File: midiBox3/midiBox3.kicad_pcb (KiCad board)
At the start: 2 copper layers, 100 x 100 mm, 117 parts, among them J1 BarrelJack, J2 DIN5 IN, J3 WaveBlaster, J4 DIN5 OUT, J5 RSA 2x, J6 STM32_PROG, J7 LED_CON, Q1 IRFL110, SW1 D_VALUE, SW2 SW_Reed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

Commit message: Changed pcb, fix issue 1
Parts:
- moved R1 12.5 mm to (120.0, 27.0)
- moved D1 4.76 mm to (121.8, 32.7), turned to 90 degrees
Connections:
- J2 pad 4: Net-(J2-Pad4) -> /MIDI_N
- J2 pad 5: /MIDI_N -> Net-(J2-Pad5)
- R1 pad 2: Net-(J2-Pad4) -> Net-(J2-Pad5)
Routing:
- net /MIDI_P: track 5.73 -> 12.1 mm
- net Net-(J2-Pad5): track 0.00 -> 4.21 mm
- net Net-(J2-Pad4): track 3.92 -> 0.00 mm
- net /MIDI_N: track 16.4 -> 18.4 mm

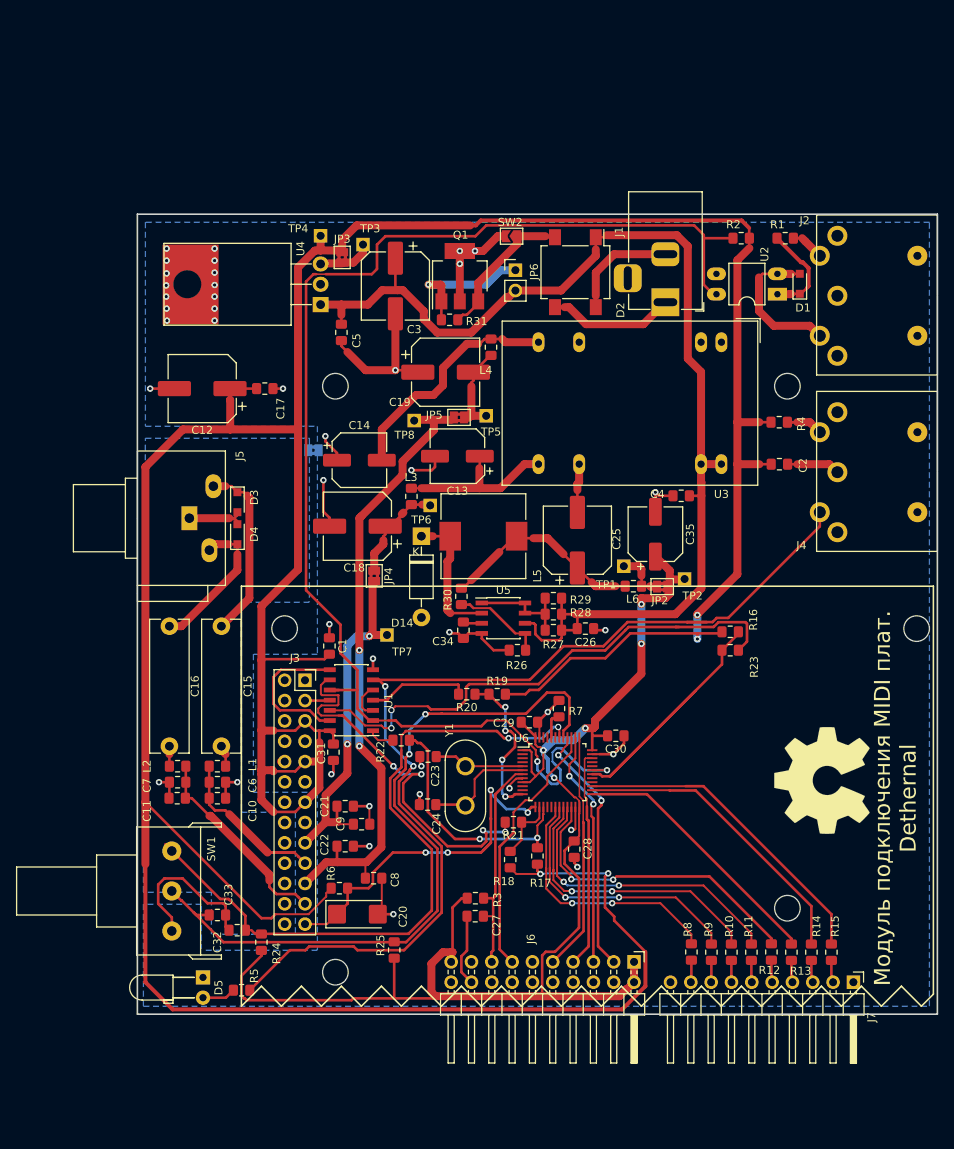
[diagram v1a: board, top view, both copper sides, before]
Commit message: Added new chip — 7404.
Because TX signals need to be inverted and MST32 lack of abilities to do so. Updated chematic and pcb.
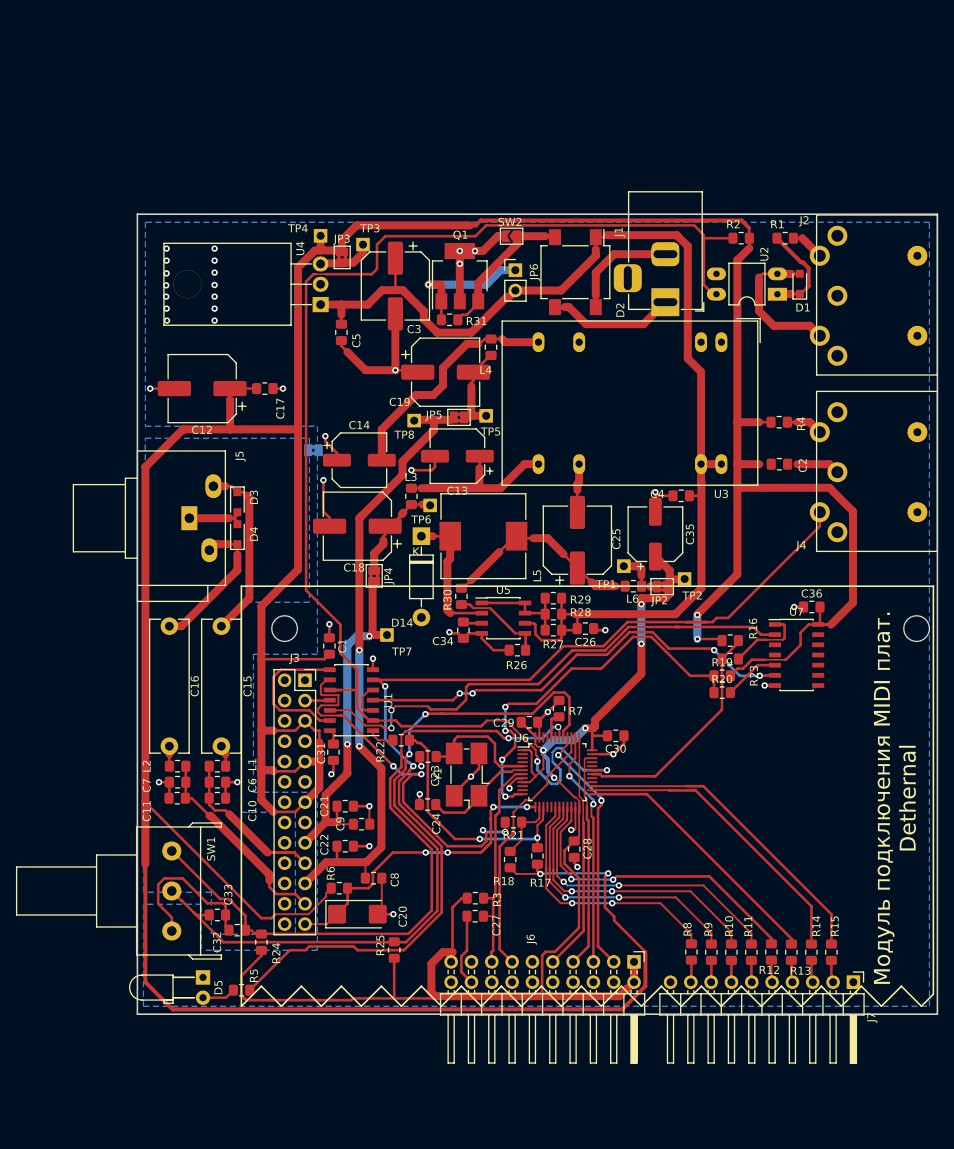
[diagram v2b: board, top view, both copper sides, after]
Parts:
- removed the REF** at (63.8, 118.8)
- removed the REF** at (63.8, 45.5)
- removed the REF** at (120.2, 45.5)
- removed the REF** at (120.2, 110.8)
- removed the REF** at (45.6, 32.8)
- removed the REF** at (124.6, 94.8)
- added C36: 100pF, Capacitor_SMD:C_0805_2012Metric_Pad1.15x1.40mm_HandSolder, F.Cu at (123.3, 73.1)
- added U7: 74ACT04, Package_SO:SOIC-14_3.9x8.7mm_P1.27mm, F.Cu at (121.4, 79.1)
- U1: value MM74HCT00M -> 74HCT00
- Y1: value 16MHz -> Crystal_GND24; footprint Crystal:Crystal_HC50_Vertical -> Crystal:Crystal_SMD_0603-4Pin_6.0x3.5mm_HandSoldering
- moved R20 31.9 mm to (112.1, 83.8), turned to 0 degrees
- moved R19 28.2 mm to (112.1, 81.7)
- moved R16 1.10 mm to (113.1, 77.3)
- moved R23 1.10 mm to (113.1, 79.6)
- moved Y1 1.06 mm to (80.2, 94.0), turned to 90 degrees
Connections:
- C2 pad 1: +5V -> GNDD
- C2 pad 2: GNDD -> +5V
- U1 pad 12: /TX1 -> Net-(U1-Pad12)
- U1 pad 4: /TX2 -> Net-(U1-Pad4)
- Y1 pad 1: Net-(C23-Pad1) -> Net-(C24-Pad1)
- Y1 pad 2: Net-(C24-Pad1) -> GNDD
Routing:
- net Net-(U1-Pad12): track 0.00 -> 65.2 mm, vias 0 -> 2
- net Net-(U1-Pad4): track 0.00 -> 56.5 mm, vias 0 -> 4
- net /TX1: track 65.4 -> 9.69 mm, vias 2 -> 0
- net Net-(R19-Pad1): track 19.6 -> 49.0 mm
- net +5V: track 494.7 -> 513.3 mm
- net Net-(R16-Pad1): track 42.2 -> 29.3 mm
- net GNDD: track 144.0 -> 151.9 mm, vias 39 -> 42
- net /TX2: track 12.8 -> 7.00 mm
- net Net-(C23-Pad1): track 11.3 -> 15.6 mm
- net /~RESET: track 45.2 -> 41.1 mm

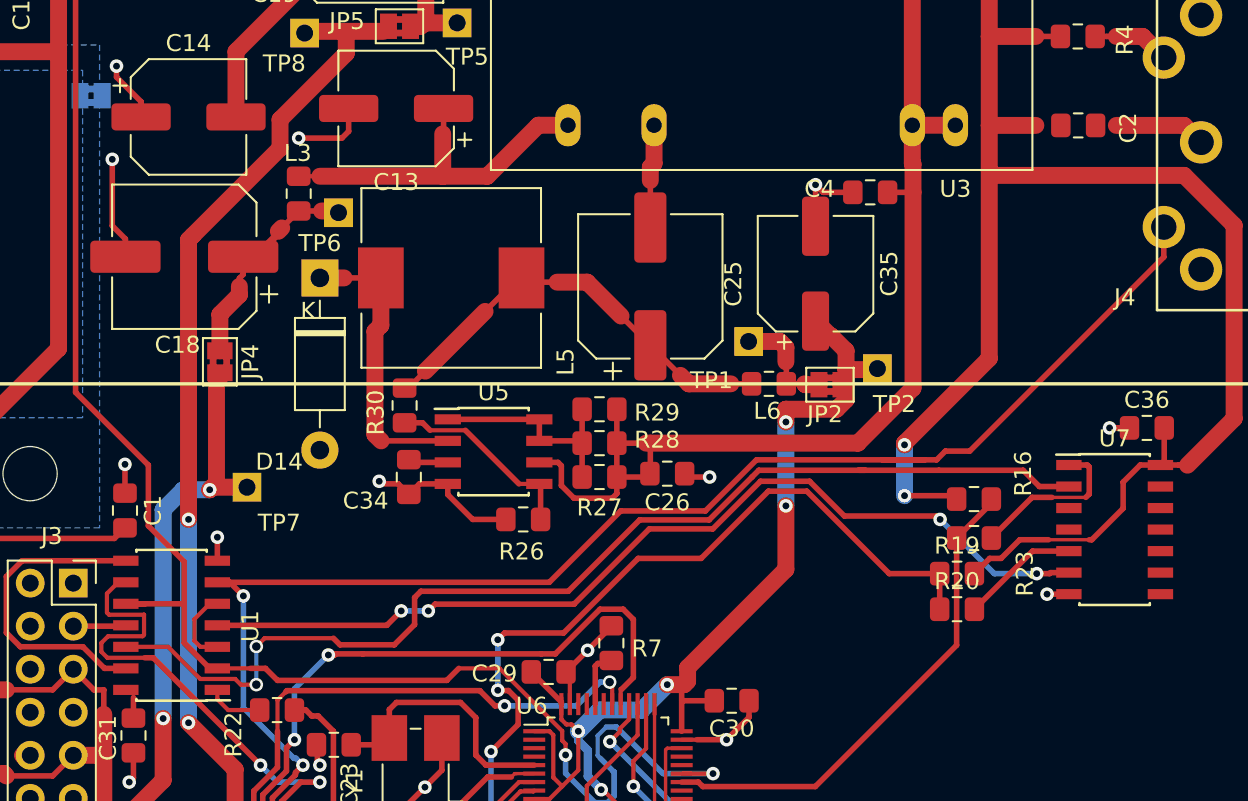
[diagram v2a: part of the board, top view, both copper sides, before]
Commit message: Replaced U2 PC817 with H11L1
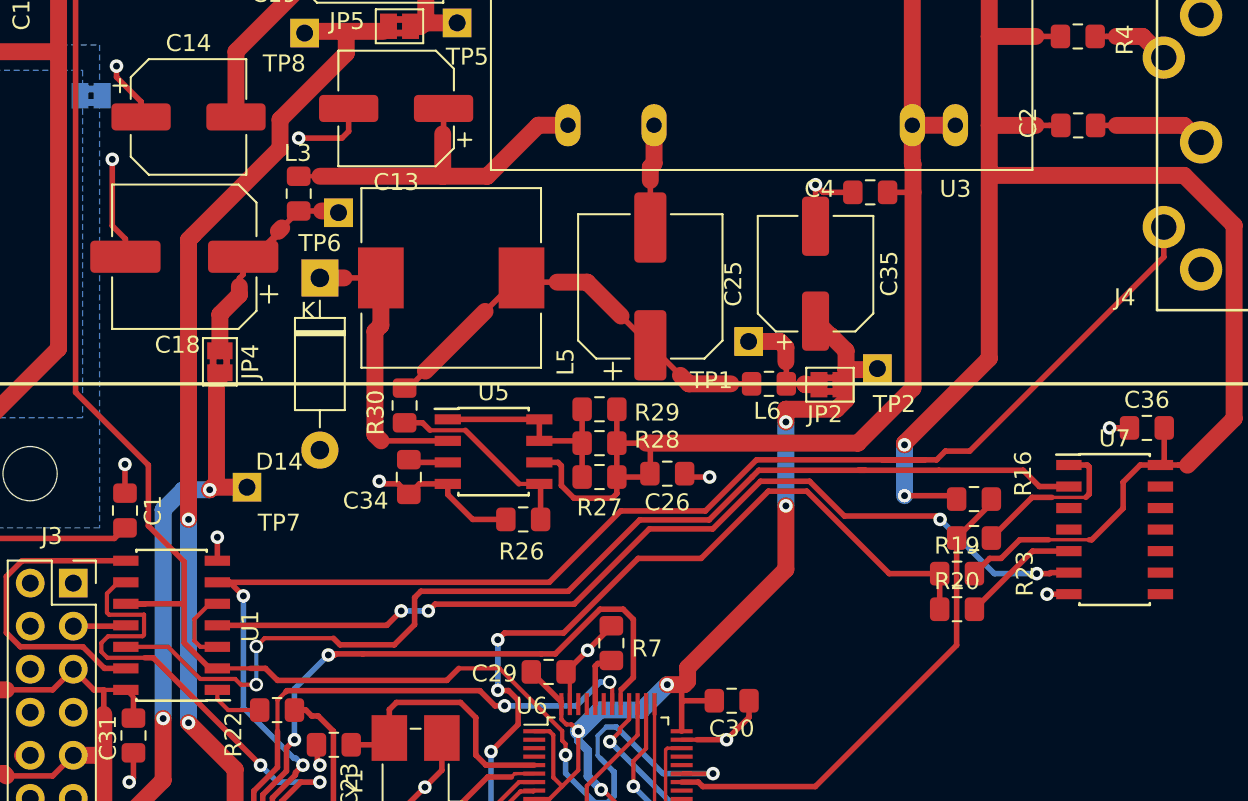
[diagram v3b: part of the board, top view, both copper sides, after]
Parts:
- turned C2 to 180 degrees
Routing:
- net +5V: track 513.3 -> 516.7 mm
- net GNDD: track 151.9 -> 153.1 mm

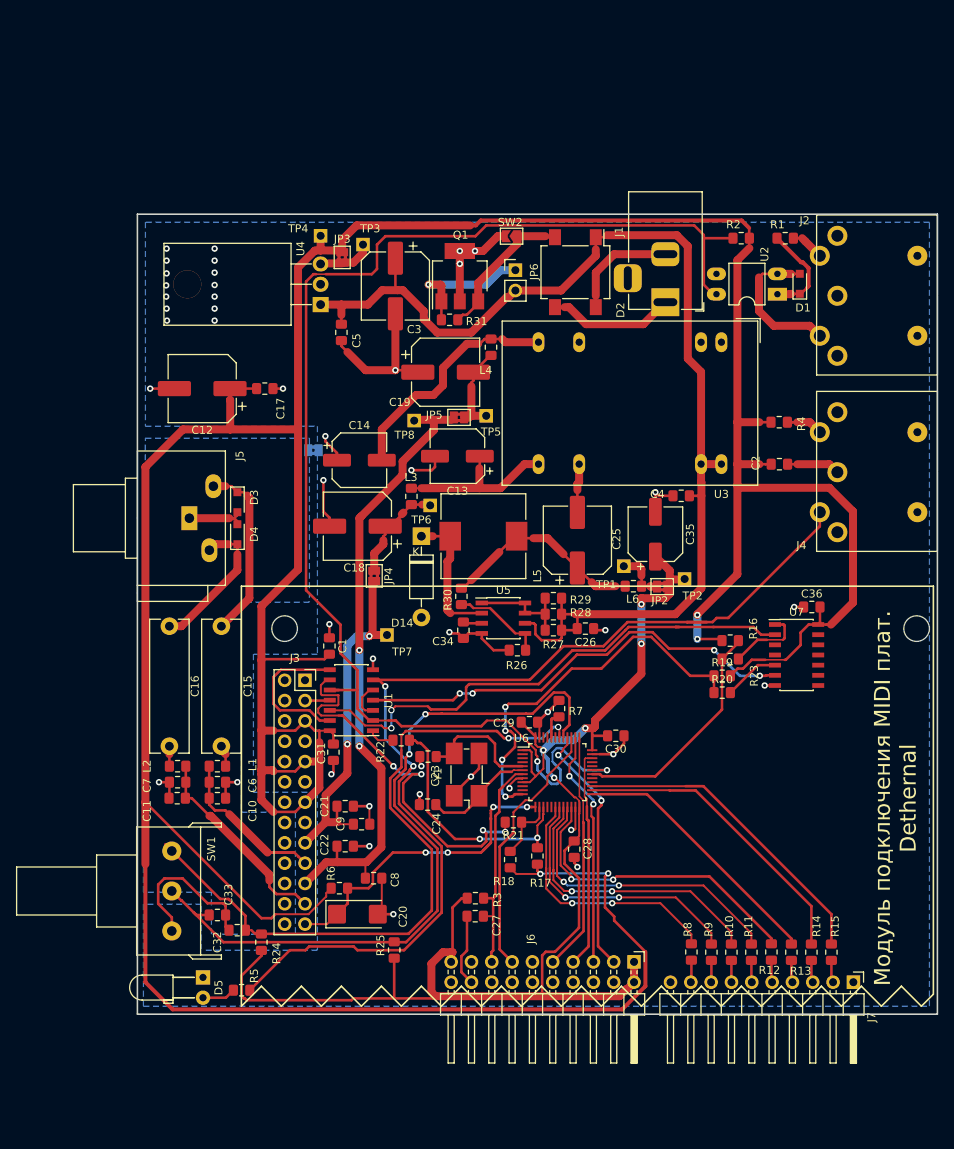
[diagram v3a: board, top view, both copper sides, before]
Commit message: Промежуточная версия. Нужно рассчиать какие дополнительные таймеры потребуются для работы.
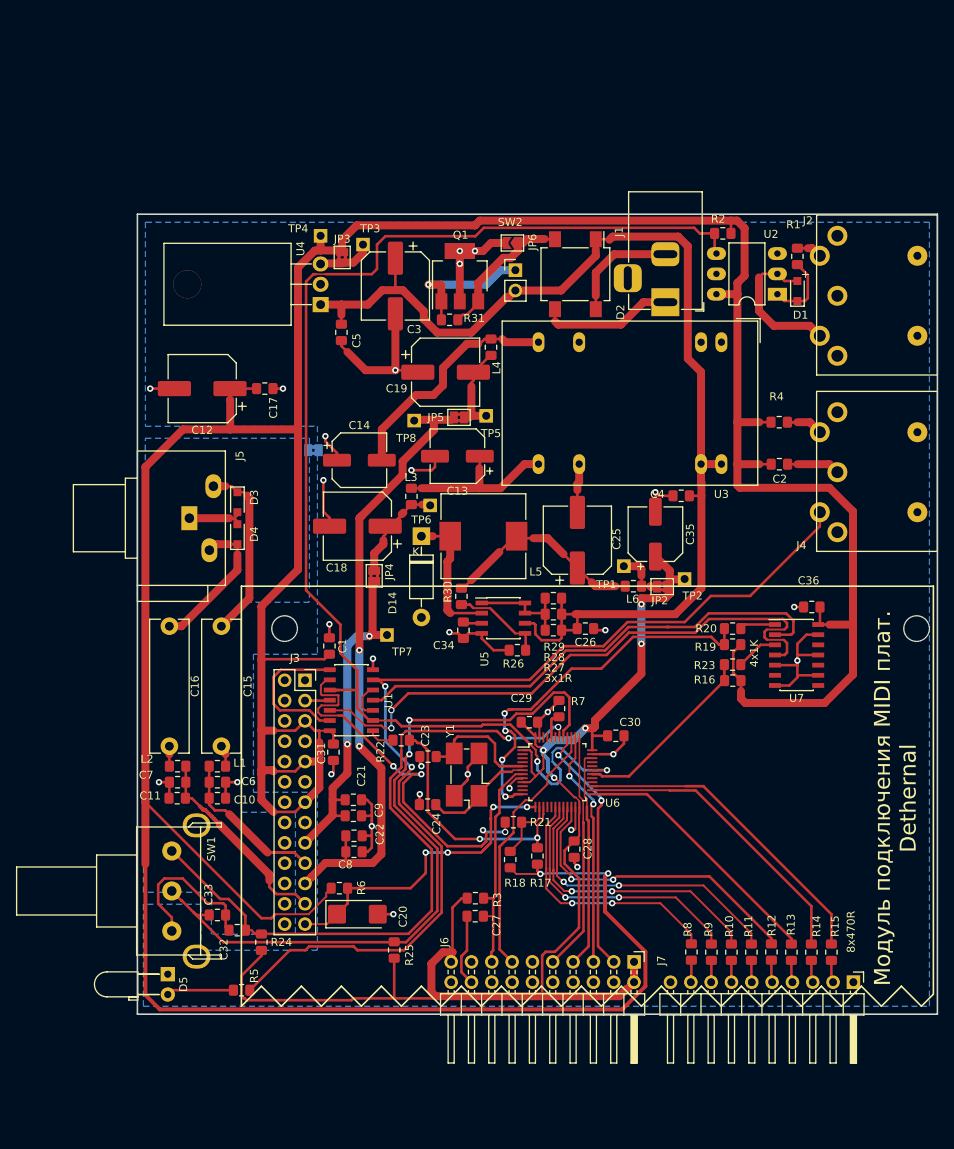
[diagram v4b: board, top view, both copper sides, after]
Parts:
- R2: value 430R ±5% -> 270R
- U2: value PC817 -> H11L1; footprint Package_DIP:DIP-4_W7.62mm_LongPads -> Package_DIP:DIP-6_W7.62mm_LongPads
- Y1: value Crystal_GND24 -> 16MHz
- moved R20 8.10 mm to (113.4, 75.8)
- moved R16 5.01 mm to (113.4, 82.3), turned to 0 degrees
- moved D5 4.42 mm to (42.8, 119.0)
- moved R19 4.11 mm to (113.4, 77.8)
- moved C8 4.11 mm to (66.1, 103.7)
- moved R1 2.74 mm to (121.5, 29.3), turned to 90 degrees
- moved R2 2.38 mm to (112.2, 26.4)
- moved C22 1.70 mm to (66.1, 101.7)
- moved C9 1.47 mm to (66.0, 99.2)
- moved C21 1.30 mm to (66.0, 97.2)
- moved D1 0.95 mm to (121.5, 33.6)
- moved JP6 0.86 mm to (85.9, 27.6)
- moved R23 0.76 mm to (113.4, 80.3)
- moved D2 0.25 mm to (93.8, 31.5)
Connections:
- U2 pad 3: GNDD -> (no net)
- U7 pad 1: /TX1 -> /TX2
- U7 pad 11: (no net) -> GNDD
- U7 pad 13: (no net) -> GNDD
- U7 pad 2: Net-(U1-Pad12) -> Net-(U1-Pad4)
- U7 pad 3: (no net) -> /TX1
- U7 pad 4: (no net) -> Net-(U1-Pad12)
- U7 pad 5: /TX2 -> GNDD
- U7 pad 6: Net-(U1-Pad4) -> (no net)
- U7 pad 9: (no net) -> GNDD
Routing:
- net GNDD: track 153.1 -> 170.7 mm, vias 42 -> 27
- net Net-(U1-Pad12): track 65.2 -> 76.6 mm
- net /MIDI_IN: track 174.0 -> 165.3 mm
- net Net-(R16-Pad1): track 29.3 -> 23.6 mm
- net Net-(U1-Pad4): track 56.5 -> 61.5 mm, vias 4 -> 0
- net /TX1: track 9.69 -> 5.30 mm
- net Net-(D5-Pad2): track 4.19 -> 8.42 mm
- net +5V: track 516.7 -> 512.7 mm, vias 4 -> 2
- net /MIDI_P: track 12.1 -> 9.04 mm
- net Net-(J4-Pad4): track 131.1 -> 128.4 mm
- net /TX2: track 7.00 -> 4.49 mm
- net +12V: track 45.0 -> 42.5 mm
- net Net-(J2-Pad5): track 4.21 -> 3.19 mm
- net Net-(D2-Pad3): track 15.8 -> 16.7 mm
- net /ENC_A: track 92.7 -> 93.5 mm
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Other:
- board text added: "+"
- board text added: "3x1R"
- board text added: "4x1K"
- board text added: "8x470R"

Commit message: Fiddling here and there.
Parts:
- added REF**: Converter_DCDC_TRACO_TMR-xxxx_THT, Converter_DCDC:Converter_DCDC_TRACO_TMR-xxxx_THT, F.Cu at (59.2, 4.50)
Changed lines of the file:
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@@
     (tracks 1182)
     (zones 0)
-    (modules 113)
+    (modules 114)
     (nets 77)
   )
@@
   )
   (setup
-    (last_trace_width 0.5)
+    (last_trace_width 0.25)
     (user_trace_width 0.2)
     (user_trace_width 0.33)
@@
     (add_net "Net-(U1-Pad4)")
   )
+  (module Converter_DCDC:Converter_DCDC_TRACO_TMR-xxxx_THT (layer F.Cu)
+    (at 59.2 4.5)
+    (descr "DCDC-Converter, TRACO, TMR xxxx, Single/Dual output, http://www.datasheetlib.com/datasheet/135136/tmr-2-2410e_traco-power.html?page=3#datasheet")
+    (tags "DCDC-Converter TRACO TMRxxxx Single/Dual_output")
+    (fp_text reference REF** (at 0 -4.24) (layer F.SilkS)
+      (effects (font (size 1 1) (thickness 0.15)))
+    )
+    (fp_text value Converter_DCDC_TRACO_TMR-xxxx_THT (at 9.5 8) (layer F.Fab)
+      (effects (font (size 1 1) (thickness 0.15)))
+    )
+    (fp_text user %R (at 9.19 3.76) (layer F.Fab)
+      (effects (font (size 1 1) (thickness 0.15)))
+    )
+    (fp_line (start -2.5 -1) (end -2.5 1) (layer F.SilkS) (width 0.12))
+    (fp_line (start -2 1) (end -1 0) (layer F.Fab) (width 0.1))
+    (fp_line (start -2 -1) (end -1 0) (layer F.Fab) (width 0.1))
+    (fp_line (start -2 -3.2) (end -2 -1) (layer F.Fab) (width 0.1))
+    (fp_line (start -2.12 -3.32) (end 19.92 -3.32) (layer F.SilkS) (width 0.12))
+    (fp_line (start 19.92 -3.32) (end 19.92 6.12) (layer F.SilkS) (width 0.12))
+    (fp_line (start 19.92 6.12) (end -2.12 6.12) (layer F.SilkS) (width 0.12))
+    (fp_line (start -2.12 6.12) (end -2.12 -3.32) (layer F.SilkS) (width 0.12))
+    (fp_line (start 20.05 -3.45) (end 20.05 6.25) (layer F.CrtYd) (width 0.05))
+    (fp_line (start -2.25 6.25) (end 20.05 6.25) (layer F.CrtYd) (width 0.05))
+    (fp_line (start 19.8 6) (end -2 6) (layer F.Fab) (width 0.1))
+    (fp_line (start 19.8 -3.2) (end 19.8 6) (layer F.Fab) (width 0.1))
+    (fp_line (start 19.8 -3.2) (end -2 -3.2) (layer F.Fab) (width 0.1))
+    (fp_line (start -2 1) (end -2 6) (layer F.Fab) (width 0.1))
+    (fp_line (start -2.25 -3.45) (end 20.05 -3.45) (layer F.CrtYd) (width 0.05))
+    (fp_line (start -2.25 -3.45) (end -2.25 6.25) (layer F.CrtYd) (width 0.05))
+    (pad 8 thru_hole oval (at 17.78 0) (size 1.5 3) (drill 1) (layers *.Cu *.Mask))
+    (pad 7 thru_hole oval (at 15.24 0) (size 1.5 3) (drill 1) (layers *.Cu *.Mask))
+    (pad 3 thru_hole oval (at 5.08 0) (size 1.5 3) (drill 1) (layers *.Cu *.Mask))
+    (pad 6 thru_hole oval (at 12.7 0) (size 1.5 3) (drill 1) (layers *.Cu *.Mask))
+    (pad 5 thru_hole oval (at 10.16 0) (size 1.5 3) (drill 1) (layers *.Cu *.Mask))
+    (pad 2 thru_hole oval (at 2.54 0) (size 1.5 3) (drill 1) (layers *.Cu *.Mask))
+    (pad 1 thru_hole rect (at 0 0) (size 1.5 3) (drill 1) (layers *.Cu *.Mask))
+    (model ${KISYS3DMOD}/Converter_DCDC.3dshapes/Converter_DCDC_TRACO_TMR-xxxx_THT.wrl
+      (at (xyz 0 0 0))
+      (scale (xyz 1 1 1))
+      (rotate (xyz 0 0 0))
+    )
+  )
   (module rotary_encoder_bourns:Rotary_Encoder_Bourns_PEC16-2215F-N0024_Horizontal_16mm (layer F.Cu)
